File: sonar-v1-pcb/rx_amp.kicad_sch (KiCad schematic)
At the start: 7 parts, among them U10 ${SIM.PARAMS}, U11 ${SIM.PARAMS}

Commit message: added some adc shit
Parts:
- added C1: 1.6nF, Capacitor_SMD:C_0201_0603Metric, symbol Device:C
- added R97: 1k, Resistor_SMD:R_0201_0603Metric, symbol Device:R_US
- R1: renamed from R13; footprint Capacitor_SMD:C_0201_0603Metric -> Resistor_SMD:R_0201_0603Metric
- R2: renamed from R14; value 290k -> 100k; footprint Capacitor_SMD:C_0201_0603Metric -> Resistor_SMD:R_0201_0603Metric
- R3: renamed from R15; footprint Capacitor_SMD:C_0201_0603Metric -> Resistor_SMD:R_0201_0603Metric
- R4: renamed from R16; value R_US -> 100k; footprint (none) -> Resistor_SMD:R_0201_0603Metric
- U2: renamed from U10; footprint (none) -> Package_TO_SOT_SMD:SOT-23-5
- U3: renamed from U11; footprint (none) -> Package_TO_SOT_SMD:SOT-23-5
- renumbered MK4 to MK1
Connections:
- net 20V is gone; now on net 10V: U2.3 (V+), U3.3 (V+)
- net 10V: no longer MK1.2 (+)
- net GND: now also MK1.2 (+), C1.2; no longer U2.4 (V-), U3.4 (V-)
- net at U2.1 (+): now also C1.1, R97.1; no longer MK1.1 (-)
- new net: MK1.1 (-), R97.2
- new net -10V: U2.4 (V-), U3.4 (V-)
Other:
- note added: "40KHz Carrier Wave"
- note added: "Low-pass Filter 100kHz"
- note removed: "BANDPASS"

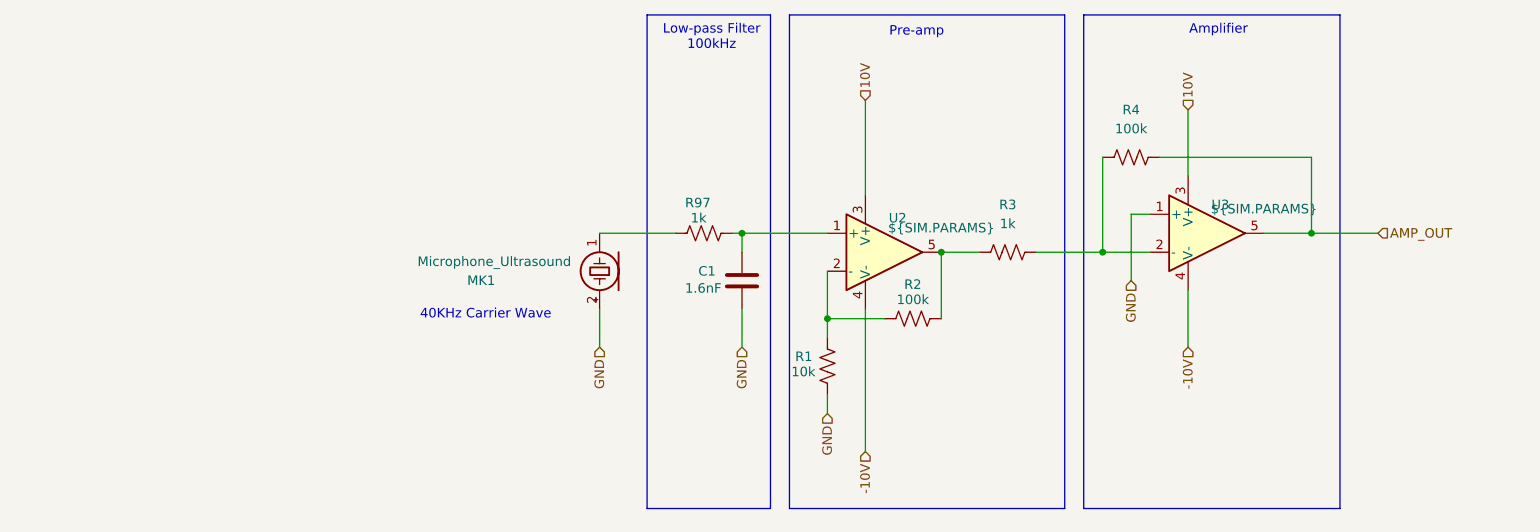
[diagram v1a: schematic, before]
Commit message: fix bandpass
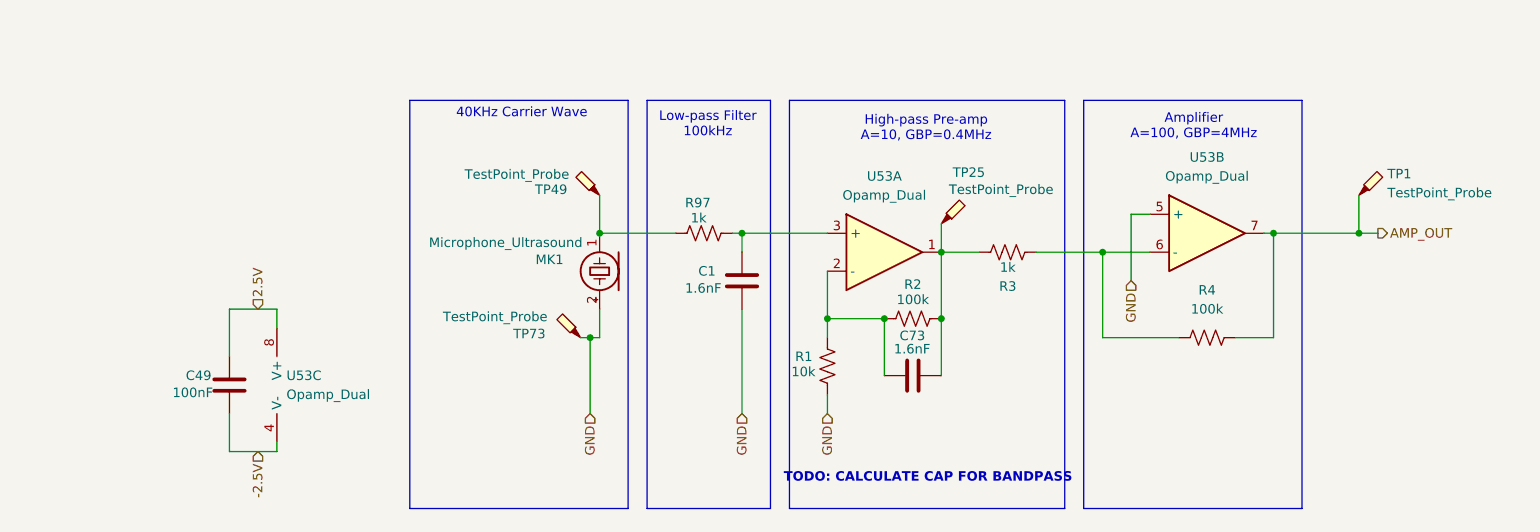
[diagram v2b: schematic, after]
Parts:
- removed U2, U3: ${SIM.PARAMS}, Package_TO_SOT_SMD:SOT-23-5, symbol Simulation_SPICE:OPAMP
- added C49: 100nF, Capacitor_SMD:C_0402_1005Metric, symbol Device:C
- added C73: 1.6nF, Capacitor_SMD:C_0402_1005Metric, symbol Device:C
- added TP1, TP25, TP49, TP73: TestPoint_Probe, TestPoint:TestPoint_Pad_D1.0mm, symbol Connector:TestPoint_Probe
- added U53: Opamp_Dual, Package_SO:TSSOP-8_3x3mm_P0.65mm, symbol Device:Opamp_Dual
- C1: footprint Capacitor_SMD:C_0201_0603Metric -> Capacitor_SMD:C_0402_1005Metric
- R1, R2, R3, R4, R97: footprint Resistor_SMD:R_0201_0603Metric -> Resistor_SMD:R_0402_1005Metric
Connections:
- net AMP_OUT: now also TP1.1, U53.7
- net GND: now also TP73.1, U53.5 (+)
- net at C1.1, R97.1: now also U53.3 (+)
- net at MK1.1 (-), R97.2: now also TP49.1
- net at R3.1, R4.1: now also U53.6 (-)
- net at R2.2, R3.2: now also C73.1, TP25.1, U53.1
- net at R1.1, R2.1: now also C73.2, U53.2 (-)
- new net -2.5V: C49.2, U53.4 (V-)
- new net 2.5V: C49.1, U53.8 (V+)
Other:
- note added: "Amplifier A=100, GBP=4MHz"
- note added: "High-pass Pre-amp A=10, GBP=0.4MHz"
- note added: "TODO: CALCULATE CAP FOR BANDPASS"
- note removed: "Amplifier"
- note removed: "Pre-amp"
- moved on the sheet: R4

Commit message: Add lowpas filter
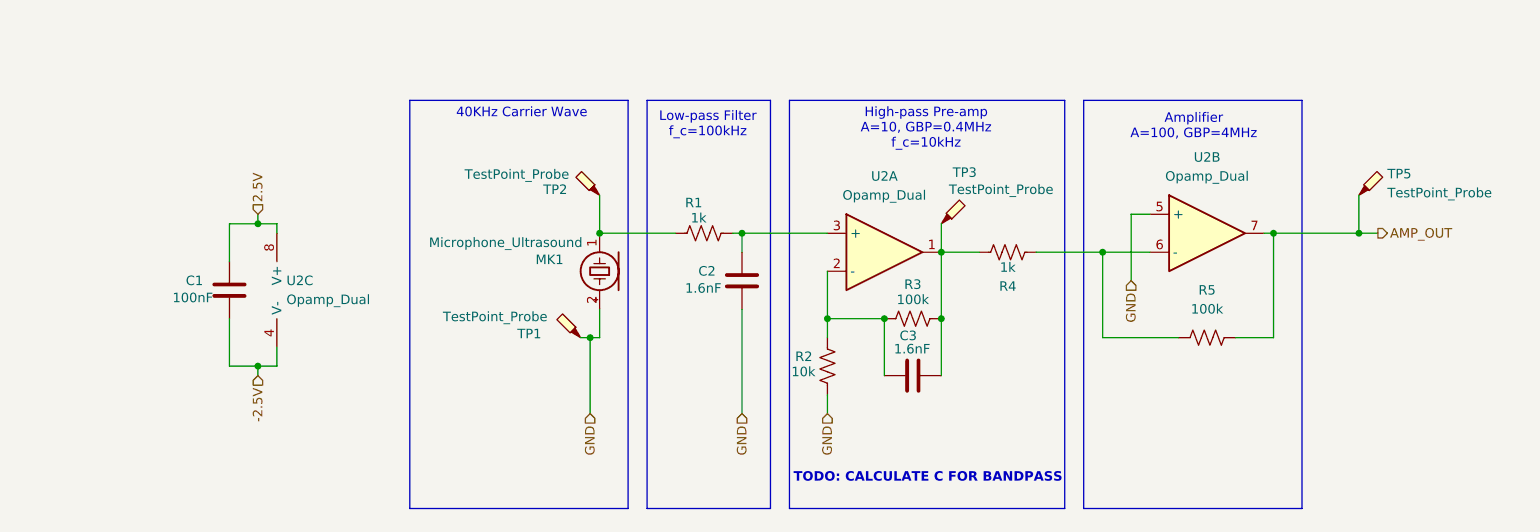
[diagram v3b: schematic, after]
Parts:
- renumbered C49 to C1, C1 to C2, C73 to C3, R97 to R1, R1 to R2, R2 to R3, R3 to R4, R4 to R5, TP73 to TP1, TP49 to TP2, TP25 to TP3, TP1 to TP5, U53 to U2
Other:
- note added: "High-pass Pre-amp A=10, GBP=0.4MHz f_c=10kHz"
- note added: "Low-pass Filter f_c=100kHz"
- note added: "TODO: CALCULATE C FOR BANDPASS"
- note removed: "High-pass Pre-amp A=10, GBP=0.4MHz"
- note removed: "Low-pass Filter 100kHz"
- note removed: "TODO: CALCULATE CAP FOR BANDPASS"
- moved on the sheet: C1, U2C

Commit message: finish ADC signals
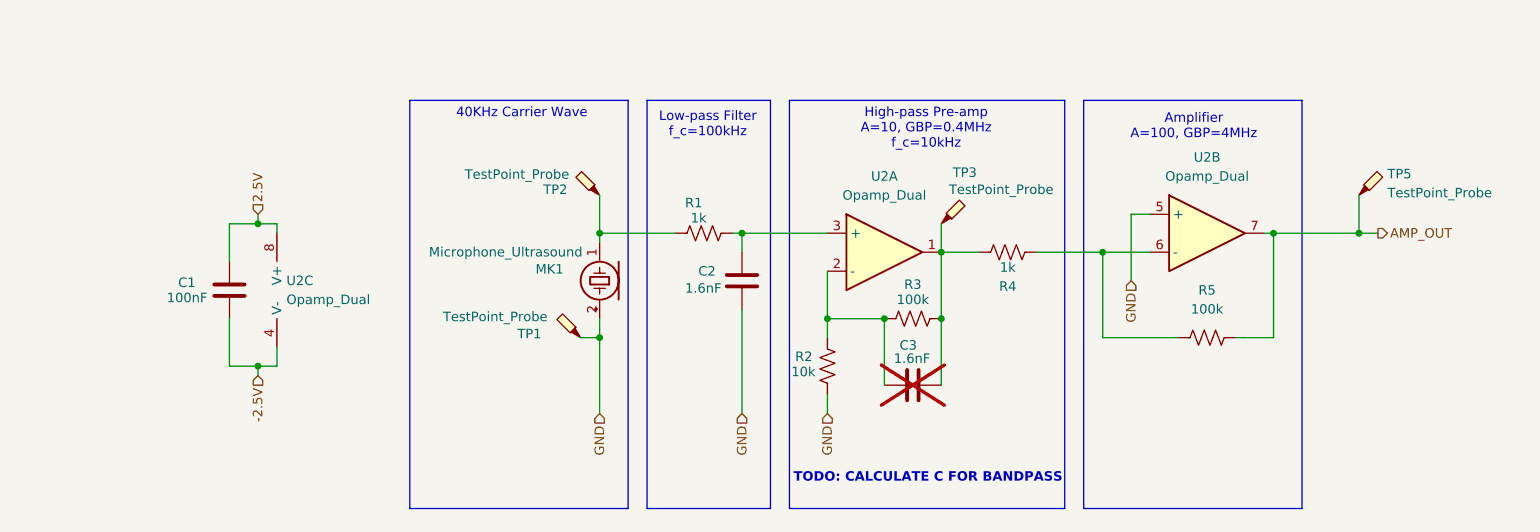
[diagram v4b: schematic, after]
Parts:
- C3: now not fitted
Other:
- moved on the sheet: MK1

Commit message: kept cooking
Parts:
- renumbered C2 to C10, C3 to C11, C1 to C9, R1 to R5, R2 to R6, R3 to R7, R4 to R8, R5 to R9, TP5 to TP4
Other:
- note added: "26 mA max draw for dual package"

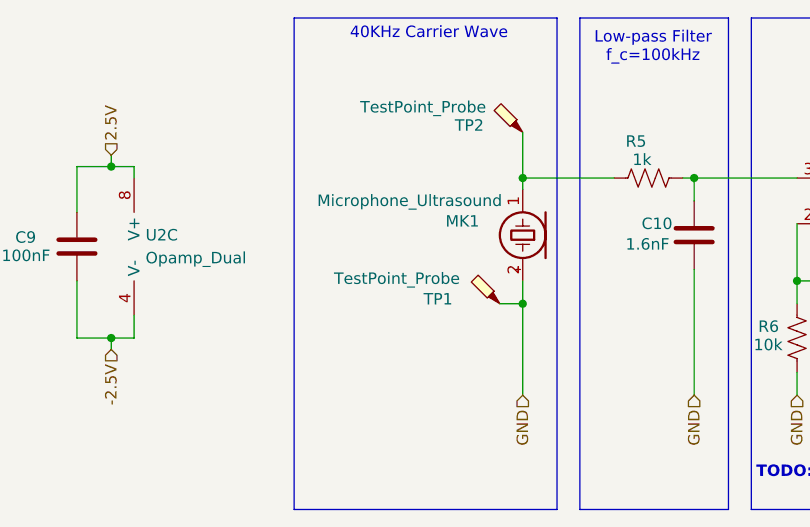
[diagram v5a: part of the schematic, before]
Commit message: Switch to audio not just ultrasonic.
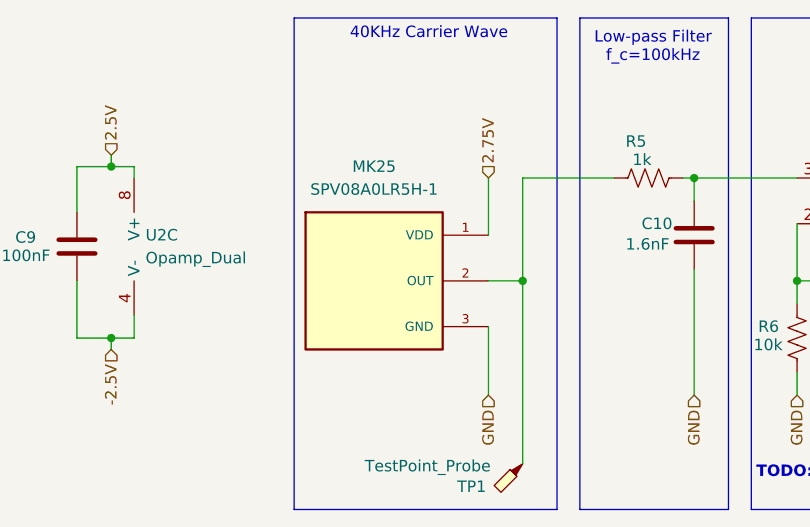
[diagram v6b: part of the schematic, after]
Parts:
- removed MK1: Microphone_Ultrasound, Sonar:MA40S4, symbol Device:Microphone_Ultrasound
- removed TP2: TestPoint_Probe, TestPoint:TestPoint_Pad_D1.0mm, symbol Connector:TestPoint_Probe
- added MK25: SPV08A0LR5H-1, Sonar:MIC_SPV08A0LR5H-1, symbol sonar_lib:SPV08A0LR5H-1
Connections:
- net GND: now also MK25.3 (GND); no longer TP1.1
- net at R5.2: now also TP1.1, MK25.2 (OUT)
- new net 2.75V: MK25.1 (VDD)

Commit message: Josh cooking some more.
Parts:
- C301: renamed from C10; value 1.6nF -> 3.3nF
- MK301: renamed from MK25; value SPV08A0LR5H-1 -> SPV0142LR5H-1
- renumbered C9 to C302, C11 to C303, R5 to R301, R8 to R302, R7 to R303, R9 to R304, R6 to R305, TP4 to TP301, TP3 to TP302, TP1 to TP303, U2 to U301
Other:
- note added: "175uA at 2.75V"
- note added: "17KHz Carrier Wave"
- note added: "Amplifier A=10, GBP=0.17MHz"
- note added: "High-pass Pre-amp A=10, GBP=0.17MHz f_c=10kHz"
- note added: "Low-pass Filter f_c=48.2kHz"
- note removed: "40KHz Carrier Wave"
- note removed: "Amplifier A=100, GBP=4MHz"
- note removed: "High-pass Pre-amp A=10, GBP=0.4MHz f_c=10kHz"
- note removed: "Low-pass Filter f_c=100kHz"
